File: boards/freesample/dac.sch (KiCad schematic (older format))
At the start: 18 parts, among them U4 LTC2664CUH-16#PBF

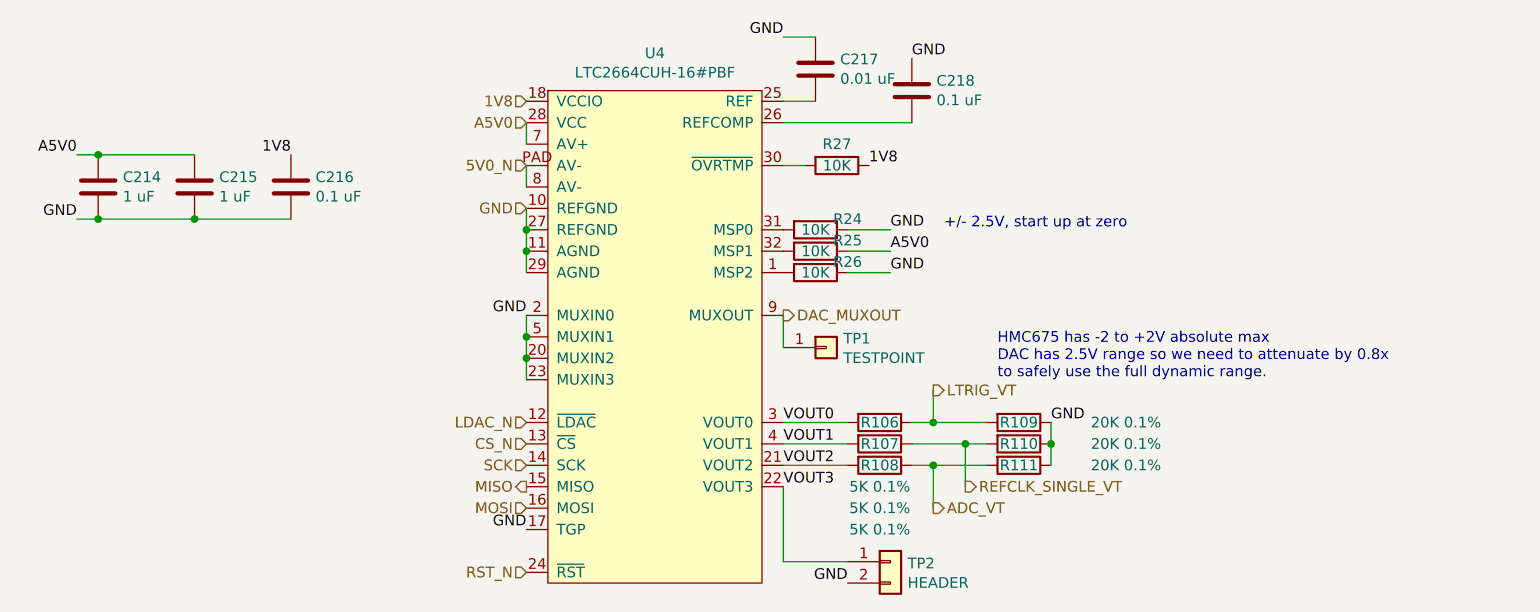
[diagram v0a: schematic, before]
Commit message: Added more test points. Started picking packages for passives. Continued schematic review.
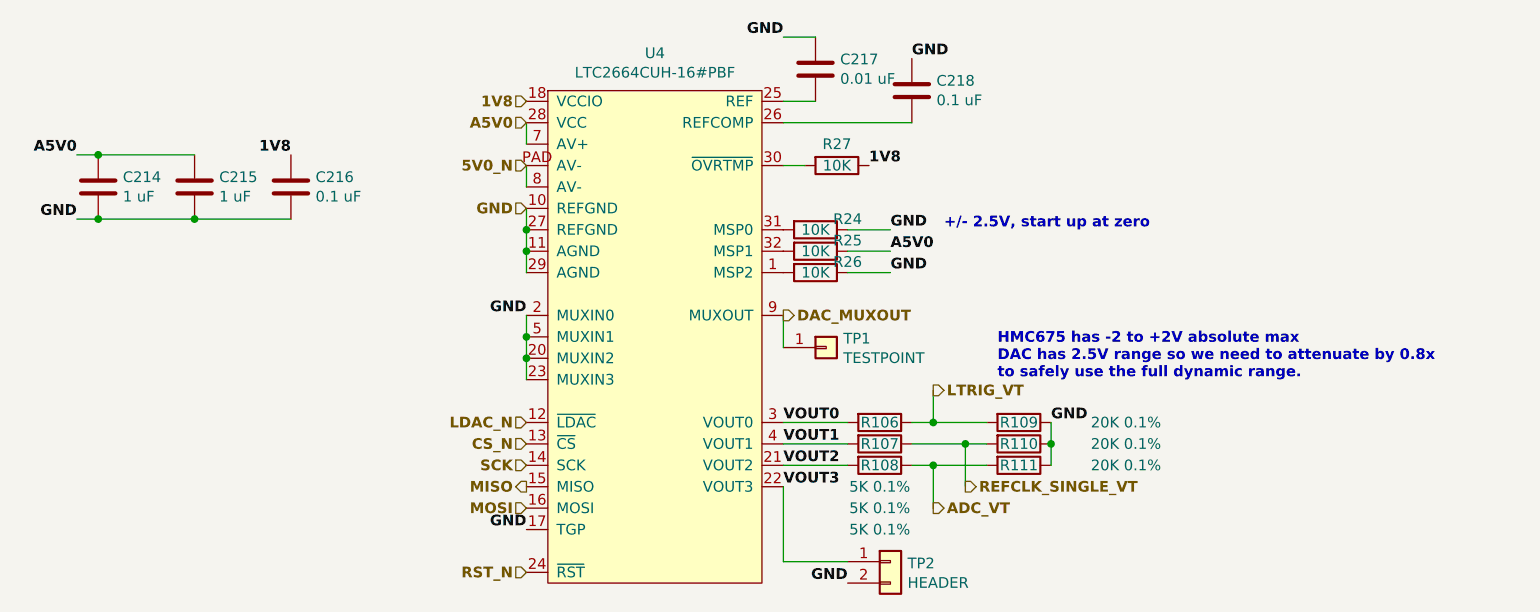
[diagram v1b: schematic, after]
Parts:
- C214, C215: footprint (none) -> azonenberg_pcb:EIA_0603_CAP_NOSILK
- C216, C217, C218: footprint (none) -> azonenberg_pcb:EIA_0402_CAP_NOSILK
- R24, R25, R26, R27: footprint (none) -> azonenberg_pcb:EIA_0402_RES_NOSILK
- TP1: footprint (none) -> azonenberg_pcb:TESTPOINT_SMT_KEYSTONE_5016
- TP2: footprint (none) -> azonenberg_pcb:CONN_HEADER_2.54MM_1x2
- U4: footprint (none) -> azonenberg_pcb:QFN_32_0.5MM_5x5MM
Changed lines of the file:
@@
 F 0 "U4" H 4650 7025 50  0000 C CNN
 F 1 "LTC2664CUH-16#PBF" H 4650 6934 50  0000 C CNN
-F 2 "" H 4150 4450 50  0001 C CNN
+F 2 "azonenberg_pcb:QFN_32_0.5MM_5x5MM" H 4150 4450 50  0001 C CNN
 F 3 "" H 4150 4450 50  0001 C CNN
 	1    4150 4450
 	1    0    0    -1
 $EndComp
-Text HLabel 5950 3450 2    50   Output ~ 0
+Text HLabel 5950 3450 2    50   Output ~ 6
 LTRIG_VT
-Text HLabel 6100 3900 2    50   Output ~ 0
+Text HLabel 6100 3900 2    50   Output ~ 6
 REFCLK_SINGLE_VT
-Text HLabel 5950 4000 2    50   Output ~ 0
+Text HLabel 5950 4000 2    50   Output ~ 6
 ADC_VT
-Text HLabel 4050 2200 0    50   Input ~ 0
+Text HLabel 4050 2200 0    50   Input ~ 6
 A5V0
-Text HLabel 4050 2400 0    50   Input ~ 0
+Text HLabel 4050 2400 0    50   Input ~ 6
 5V0_N
-Text HLabel 4050 2600 0    50   Input ~ 0
-GND
-Text HLabel 5250 3100 2    50   Output ~ 0
+Text HLabel 4050 2600 0    50   Input ~ 6
+GND
+Text HLabel 5250 3100 2    50   Output ~ 6
 DAC_MUXOUT
-Text HLabel 4050 3600 0    50   Input ~ 0
+Text HLabel 4050 3600 0    50   Input ~ 6
 LDAC_N
-Text HLabel 4050 3700 0    50   Input ~ 0
+Text HLabel 4050 3700 0    50   Input ~ 6
 CS_N
-Text HLabel 4050 3800 0    50   Input ~ 0
+Text HLabel 4050 3800 0    50   Input ~ 6
 SCK
-Text HLabel 4050 4000 0    50   Input ~ 0
+Text HLabel 4050 4000 0    50   Input ~ 6
 MOSI
-Text HLabel 4050 3900 0    50   Output ~ 0
+Text HLabel 4050 3900 0    50   Output ~ 6
 MISO
-Text HLabel 4050 4300 0    50   Input ~ 0
+Text HLabel 4050 4300 0    50   Input ~ 6
 RST_N
-Text HLabel 4050 2100 0    50   Input ~ 0
+Text HLabel 4050 2100 0    50   Input ~ 6
 1V8
 Wire Wire Line
@@
 Wire Wire Line
 	4050 2800 4050 2900
-Text Label 4050 3100 2    50   ~ 0
+Text Label 4050 3100 2    50   ~ 6
 GND
 Wire Wire Line
@@
 F 0 "C214" H 2165 2546 50  0000 L CNN
 F 1 "1 uF" H 2165 2455 50  0000 L CNN
-F 2 "" H 2088 2350 50  0001 C CNN
+F 2 "azonenberg_pcb:EIA_0603_CAP_NOSILK" H 2088 2350 50  0001 C CNN
 F 3 "" H 2050 2500 50  0001 C CNN
 	1    2050 2500
 	1    0    0    -1
 $EndComp
-Text Label 1950 2350 2    50   ~ 0
+Text Label 1950 2350 2    50   ~ 6
 A5V0
-Text Label 1950 2650 2    50   ~ 0
+Text Label 1950 2650 2    50   ~ 6
 GND
 Wire Wire Line
@@
 F 0 "C216" H 3065 2546 50  0000 L CNN
 F 1 "0.1 uF" H 3065 2455 50  0000 L CNN
-F 2 "" H 2988 2350 50  0001 C CNN
+F 2 "azonenberg_pcb:EIA_0402_CAP_NOSILK" H 2988 2350 50  0001 C CNN
 F 3 "" H 2950 2500 50  0001 C CNN
 	1    2950 2500
 	1    0    0    -1
 $EndComp
-Text Label 2950 2350 2    50   ~ 0
+Text Label 2950 2350 2    50   ~ 6
 1V8
 Wire Wire Line
@@
 F 0 "C217" H 5515 1996 50  0000 L CNN
 F 1 "0.01 uF" H 5515 1905 50  0000 L CNN
-F 2 "" H 5438 1800 50  0001 C CNN
+F 2 "azonenberg_pcb:EIA_0402_CAP_NOSILK" H 5438 1800 50  0001 C CNN
 F 3 "" H 5400 1950 50  0001 C CNN
 	1    5400 1950
@@
 Wire Wire Line
 	5400 2100 5250 2100
-Text Label 5250 1800 2    50   ~ 0
+Text Label 5250 1800 2    50   ~ 6
 GND
 Wire Wire Line
@@
 F 0 "C218" H 5965 2096 50  0000 L CNN
 F 1 "0.1 uF" H 5965 2005 50  0000 L CNN
-F 2 "" H 5888 1900 50  0001 C CNN
+F 2 "azonenberg_pcb:EIA_0402_CAP_NOSILK" H 5888 1900 50  0001 C CNN
 F 3 "" H 5850 2050 50  0001 C CNN
 	1    5850 2050
@@
 Wire Wire Line
 	5250 2200 5850 2200
-Text Label 5850 1900 0    50   ~ 0
+Text Label 5850 1900 0    50   ~ 6
 GND
 $Comp
@@
 F 0 "C215" H 2615 2546 50  0000 L CNN
 F 1 "1 uF" H 2615 2455 50  0000 L CNN
-F 2 "" H 2538 2350 50  0001 C CNN
+F 2 "azonenberg_pcb:EIA_0603_CAP_NOSILK" H 2538 2350 50  0001 C CNN
 F 3 "" H 2500 2500 50  0001 C CNN
 	1    2500 2500
@@
 F 0 "R27" V 5400 2400 50  0000 C CNN
 F 1 "10K" V 5500 2400 50  0000 C CNN
-F 2 "" V 5430 2400 50  0001 C CNN
+F 2 "azonenberg_pcb:EIA_0402_RES_NOSILK" V 5430 2400 50  0001 C CNN
 F 3 "" H 5500 2400 50  0001 C CNN
 	1    5500 2400
@@
 Wire Wire Line
 	5350 2400 5250 2400
-Text Label 5650 2400 0    50   ~ 0
+Text Label 5650 2400 0    50   ~ 6
 1V8
-Text Label 5750 2700 0    50   ~ 0
+Text Label 5750 2700 0    50   ~ 6
 GND
 $Comp
@@
 F 0 "R24" V 5350 2850 50  0000 C CNN
 F 1 "10K" V 5400 2700 50  0000 C CNN
-F 2 "" V 5330 2700 50  0001 C CNN
+F 2 "azonenberg_pcb:EIA_0402_RES_NOSILK" V 5330 2700 50  0001 C CNN
 F 3 "" H 5400 2700 50  0001 C CNN
 	1    5400 2700
@@
 Wire Wire Line
 	5550 2700 5750 2700
-Text Label 5750 2900 0    50   ~ 0
+Text Label 5750 2900 0    50   ~ 6
 GND
 $Comp
@@
 F 0 "R26" V 5350 3050 50  0000 C CNN
 F 1 "10K" V 5400 2900 50  0000 C CNN
-F 2 "" V 5330 2900 50  0001 C CNN
+F 2 "azonenberg_pcb:EIA_0402_RES_NOSILK" V 5330 2900 50  0001 C CNN
 F 3 "" H 5400 2900 50  0001 C CNN
 	1    5400 2900
@@
 Wire Wire Line
 	5550 2900 5750 2900
-Text Label 5750 2800 0    50   ~ 0
+Text Label 5750 2800 0    50   ~ 6
 A5V0
 $Comp
@@
 F 0 "R25" V 5350 2950 50  0000 C CNN
 F 1 "10K" V 5400 2800 50  0000 C CNN
-F 2 "" V 5330 2800 50  0001 C CNN
+F 2 "azonenberg_pcb:EIA_0402_RES_NOSILK" V 5330 2800 50  0001 C CNN
 F 3 "" H 5400 2800 50  0001 C CNN
 	1    5400 2800
@@
 Wire Wire Line
 	5550 2800 5750 2800
-Text Notes 6000 2700 0    50   ~ 0
+Text Notes 6000 2700 0    50   ~ 6
 +/- 2.5V, start up at zero
-Text Label 4050 4100 2    50   ~ 0
-GND
-Text Notes 6250 3400 0    50   ~ 0
+Text Label 4050 4100 2    50   ~ 6
+GND
+Text Notes 6250 3400 0    50   ~ 6
 HMC675 has -2 to +2V absolute max\nDAC has 2.5V range so we need to attenuate by 0.8x\nto safely use the full dynamic range.
 $Comp
@@
 	0    1    1    0
 $EndComp
-Text Label 5250 3600 0    50   ~ 0
+Text Label 5250 3600 0    50   ~ 6
 VOUT0
-Text Label 5250 3700 0    50   ~ 0
+Text Label 5250 3700 0    50   ~ 6
 VOUT1
-Text Label 5250 3800 0    50   ~ 0
+Text Label 5250 3800 0    50   ~ 6
 VOUT2
 Wire Wire Line
@@
 	0    1    1    0
 $EndComp
-Text Label 6500 3600 0    50   ~ 0
+Text Label 6500 3600 0    50   ~ 6
 GND
 Wire Wire Line
@@
 Wire Wire Line
 	5950 3800 6200 3800
-Text Label 5250 3900 0    50   ~ 0
+Text Label 5250 3900 0    50   ~ 6
 VOUT3
 $Comp
@@
 F 0 "TP2" H 5830 4242 50  0000 L CNN
 F 1 "HEADER" H 5830 4151 50  0000 L CNN
-F 2 "" H 5750 4250 50  0001 C CNN
+F 2 "azonenberg_pcb:CONN_HEADER_2.54MM_1x2" H 5750 4250 50  0001 C CNN
 F 3 "~" H 5750 4250 50  0001 C CNN
 	1    5750 4250
@@
 Wire Wire Line
 	5250 4250 5550 4250
-Text Label 5550 4350 2    50   ~ 0
+Text Label 5550 4350 2    50   ~ 6
 GND
 $Comp
@@
 F 0 "TP1" H 5530 3292 50  0000 L CNN
 F 1 "TESTPOINT" H 5530 3201 50  0000 L CNN
-F 2 "" H 5450 3250 50  0001 C CNN
+F 2 "azonenberg_pcb:TESTPOINT_SMT_KEYSTONE_5016" H 5450 3250 50  0001 C CNN
 F 3 "~" H 5450 3250 50  0001 C CNN
 	1    5450 3250

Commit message: Continued assigning footprints
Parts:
- R106, R107, R108, R109, R110, R111: footprint (none) -> azonenberg_pcb:EIA_0402_RES_NOSILK
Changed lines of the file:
@@
 Sheet 3 12
 Title "FREESAMPLE Oscilloscope"
-Date "2019-03-15"
+Date "2019-03-16"
 Rev "0.1"
 Comp "Andrew D. Zonenberg / Antikernel Labs"
@@
 F 0 "R106" V 5700 3600 50  0000 C CNN
 F 1 "5K 0.1%" V 6000 3600 50  0000 C CNN
-F 2 "" V 5630 3600 50  0001 C CNN
+F 2 "azonenberg_pcb:EIA_0402_RES_NOSILK" V 5630 3600 50  0001 C CNN
 F 3 "" H 5700 3600 50  0001 C CNN
 	1    5700 3600
@@
 F 0 "R107" V 5700 3700 50  0000 C CNN
 F 1 "5K 0.1%" V 6000 3700 50  0000 C CNN
-F 2 "" V 5630 3700 50  0001 C CNN
+F 2 "azonenberg_pcb:EIA_0402_RES_NOSILK" V 5630 3700 50  0001 C CNN
 F 3 "" H 5700 3700 50  0001 C CNN
 	1    5700 3700
@@
 F 0 "R108" V 5700 3800 50  0000 C CNN
 F 1 "5K 0.1%" V 6000 3800 50  0000 C CNN
-F 2 "" V 5630 3800 50  0001 C CNN
+F 2 "azonenberg_pcb:EIA_0402_RES_NOSILK" V 5630 3800 50  0001 C CNN
 F 3 "" H 5700 3800 50  0001 C CNN
 	1    5700 3800
@@
 F 0 "R109" V 6350 3600 50  0000 C CNN
 F 1 "20K 0.1%" V 6350 4100 50  0000 C CNN
-F 2 "" V 6280 3600 50  0001 C CNN
+F 2 "azonenberg_pcb:EIA_0402_RES_NOSILK" V 6280 3600 50  0001 C CNN
 F 3 "" H 6350 3600 50  0001 C CNN
 	1    6350 3600
@@
 F 0 "R110" V 6350 3700 50  0000 C CNN
 F 1 "20K 0.1%" V 6350 4200 50  0000 C CNN
-F 2 "" V 6280 3700 50  0001 C CNN
+F 2 "azonenberg_pcb:EIA_0402_RES_NOSILK" V 6280 3700 50  0001 C CNN
 F 3 "" H 6350 3700 50  0001 C CNN
 	1    6350 3700
@@
 F 0 "R111" V 6350 3800 50  0000 C CNN
 F 1 "20K 0.1%" V 6350 4300 50  0000 C CNN
-F 2 "" V 6280 3800 50  0001 C CNN
+F 2 "azonenberg_pcb:EIA_0402_RES_NOSILK" V 6280 3800 50  0001 C CNN
 F 3 "" H 6350 3800 50  0001 C CNN
 	1    6350 3800

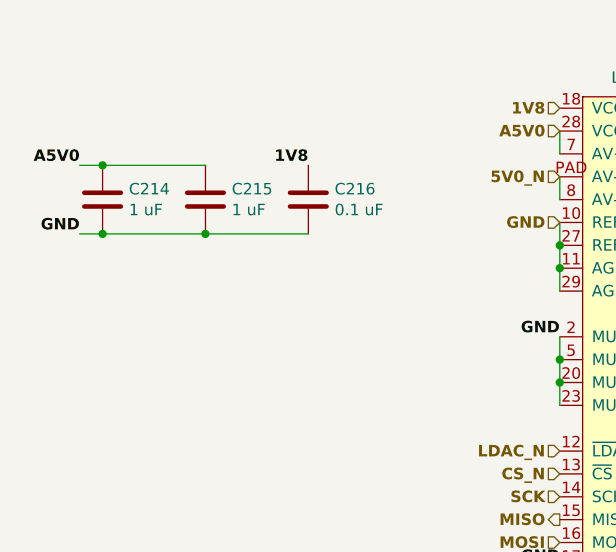
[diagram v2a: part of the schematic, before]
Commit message: Continued schematic review. Added more decoupling to DAC
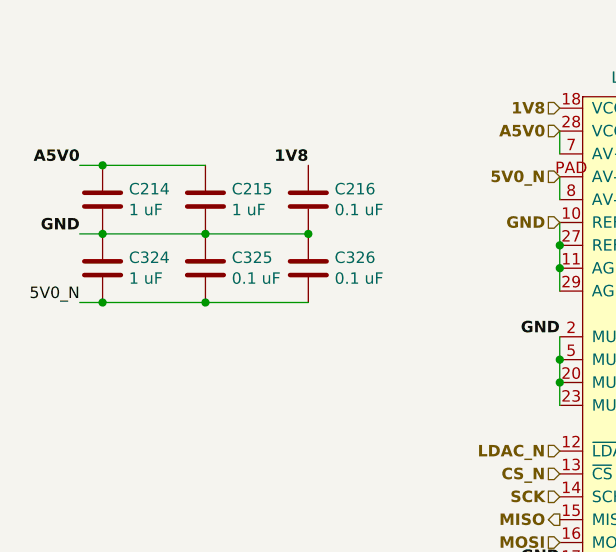
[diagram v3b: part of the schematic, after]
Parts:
- added C324: 1 uF, azonenberg_pcb:EIA_0603_CAP_NOSILK, symbol device:C
- added C325, C326: 0.1 uF, azonenberg_pcb:EIA_0402_CAP_NOSILK, symbol device:C
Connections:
- net 5V0_N: now also C324.2, C325.2, C326.2
- net GND: now also C324.1, C325.1, C326.1
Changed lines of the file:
@@
 Wire Wire Line
 	5250 3900 5250 4250
+$Comp
+L device:C C324
+U 1 1 5CB723E1
+P 2050 2800
+F 0 "C324" H 2165 2846 50  0000 L CNN
+F 1 "1 uF" H 2165 2755 50  0000 L CNN
+F 2 "azonenberg_pcb:EIA_0603_CAP_NOSILK" H 2088 2650 50  0001 C CNN
+F 3 "" H 2050 2800 50  0001 C CNN
+	1    2050 2800
+	1    0    0    -1
+$EndComp
+$Comp
+L device:C C325
+U 1 1 5CB728C4
+P 2500 2800
+F 0 "C325" H 2615 2846 50  0000 L CNN
+F 1 "0.1 uF" H 2615 2755 50  0000 L CNN
+F 2 "azonenberg_pcb:EIA_0402_CAP_NOSILK" H 2538 2650 50  0001 C CNN
+F 3 "" H 2500 2800 50  0001 C CNN
+	1    2500 2800
+	1    0    0    -1
+$EndComp
+Text Label 1950 2950 2    50   ~ 0
+5V0_N
+$Comp
+L device:C C326
+U 1 1 5CB751CD
+P 2950 2800
+F 0 "C326" H 3065 2846 50  0000 L CNN
+F 1 "0.1 uF" H 3065 2755 50  0000 L CNN
+F 2 "azonenberg_pcb:EIA_0402_CAP_NOSILK" H 2988 2650 50  0001 C CNN
+F 3 "" H 2950 2800 50  0001 C CNN
+	1    2950 2800
+	1    0    0    -1
+$EndComp
+Connection ~ 2950 2650
+Wire Wire Line
+	2950 2950 2500 2950
+Connection ~ 2500 2950
+Wire Wire Line
+	2500 2950 2050 2950
+Wire Wire Line
+	1950 2950 2050 2950
+Connection ~ 2050 2950
 $EndSCHEMATC

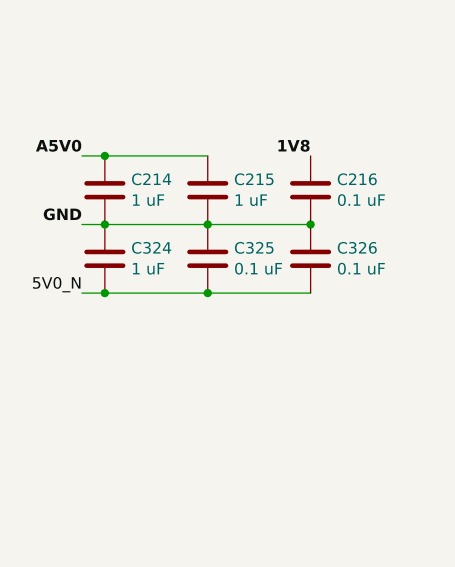
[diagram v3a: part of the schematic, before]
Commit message: Continued schematic review. Significantly simplified one-shot to reduce jitter, board area, and power consumption
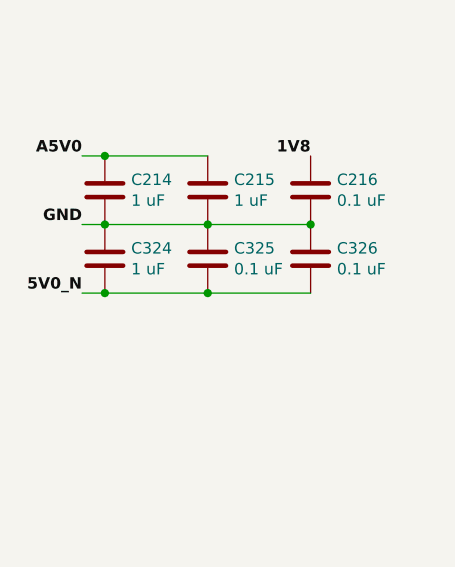
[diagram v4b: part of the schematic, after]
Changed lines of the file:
@@
 	1    0    0    -1
 $EndComp
-Text Label 1950 2950 2    50   ~ 0
+Text Label 1950 2950 2    50   ~ 6
 5V0_N
 $Comp

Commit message: Continued design review. Changed termination on DFFs to 1V8. Added some pull resistors to keep DFFs in reset during boot.
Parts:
- added R137: 10K, azonenberg_pcb:EIA_0402_RES_NOSILK, symbol device:R
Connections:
- net GND: now also R137.2
- net RST_N: now also R137.1
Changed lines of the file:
@@
 Sheet 3 12
 Title "FREESAMPLE Oscilloscope"
-Date "2019-03-16"
+Date "2019-03-17"
 Rev "0.1"
 Comp "Andrew D. Zonenberg / Antikernel Labs"
@@
 	1950 2950 2050 2950
 Connection ~ 2050 2950
+$Comp
+L device:R R137
+U 1 1 5D1127C4
+P 2600 3450
+F 0 "R137" V 2500 3450 50  0000 C CNN
+F 1 "10K" V 2600 3450 50  0000 C CNN
+F 2 "azonenberg_pcb:EIA_0402_RES_NOSILK" V 2530 3450 50  0001 C CNN
+F 3 "" H 2600 3450 50  0001 C CNN
+	1    2600 3450
+	0    1    1    0
+$EndComp
+Text Label 2450 3450 2    50   ~ 0
+GND
+Text Label 2750 3450 0    50   ~ 0
+RST_N
 $EndSCHEMATC

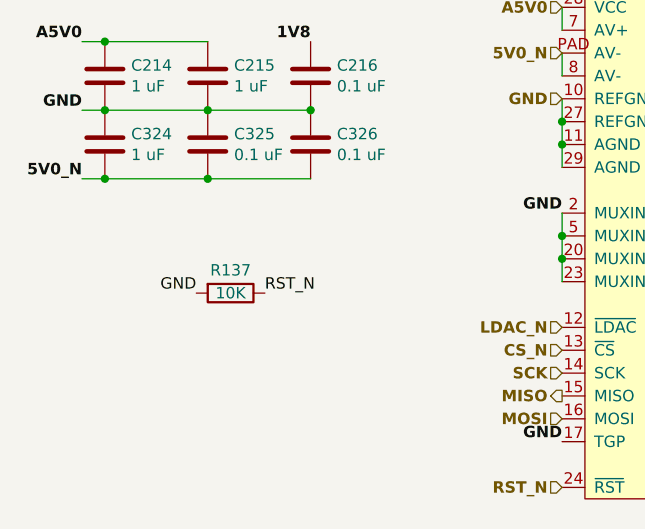
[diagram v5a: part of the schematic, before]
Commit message: Added fiducials
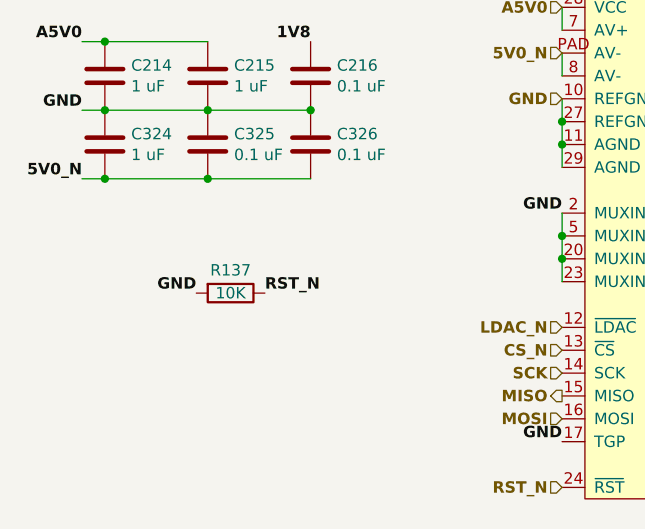
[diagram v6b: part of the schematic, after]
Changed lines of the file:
@@
 	0    1    1    0
 $EndComp
-Text Label 2450 3450 2    50   ~ 0
+Text Label 2450 3450 2    50   ~ 6
 GND
-Text Label 2750 3450 0    50   ~ 0
+Text Label 2750 3450 0    50   ~ 6
 RST_N
 $EndSCHEMATC
